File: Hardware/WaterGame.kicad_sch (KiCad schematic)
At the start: 15 parts, among them J1C1 Conn_01x07, J2 Conn_02x04_Counter_Clockwise, J4 Conn_01x02, U1 LM7805_TO220, U3 Teensy2.0_(Arduino), U4 ESP-01v090

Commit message: Hardware: Final PCB
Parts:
- removed J2: Conn_02x04_Counter_Clockwise, symbol Connector_Generic:Conn_02x04_Counter_Clockwise
- added J2: (no value), symbol Connector_Generic:Conn_02x04_Odd_Even
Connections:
- net at U6.11 (3Y): now also J2.3 (Pin_3)
- net at J1C1.1 (Pin_1), J1C1.2 (Pin_2), J1C1.3 (Pin_3)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: now also U2.1 (VI); no longer U2.2 (GND)
- net at U6.14 (4Y): now also J2.4 (Pin_4)
- net at U6.3 (1Y): now also J2.1 (Pin_1)
- net at U6.6 (2Y): now also J2.2 (Pin_2)
- net at J3.1 (Pin_1), U1.1 (VI), U5.8 (VCC2)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: now also U2.3 (VO); no longer U2.1 (VI)
- net at U5.3 (1Y): now also J2.5 (Pin_5)
- net at U5.11 (3Y): now also J2.7 (Pin_7)
- net at U5.14 (4Y): now also J2.8 (Pin_8)
- net at U5.6 (2Y): now also J2.6 (Pin_6)
- net at J5A2.4 (Pin_4), R1.2, U4.3 (CH_PD)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: now also U2.2 (GND); no longer U2.3 (VO)
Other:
- moved on the sheet: U2
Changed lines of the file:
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@@
   (junction (at 134.62 49.53) (diameter 0) (color 0 0 0 0)
   )
+  (junction (at 63.5 81.28) (diameter 0) (color 0 0 0 0)
+  )
   (junction (at 86.36 95.25) (diameter 0) (color 0 0 0 0)
   )
@@
   (junction (at 72.39 104.14) (diameter 0) (color 0 0 0 0)
   )
-  (junction (at 48.26 81.28) (diameter 0) (color 0 0 0 0)
-  )
   (junction (at 67.31 106.68) (diameter 0) (color 0 0 0 0)
   )
@@
   (junction (at 71.12 81.28) (diameter 0) (color 0 0 0 0)
   )
+  (junction (at 55.88 78.74) (diameter 0) (color 0 0 0 0)
+  )
   (junction (at 137.16 54.61) (diameter 0) (color 0 0 0 0)
   )
@@
   (junction (at 137.16 49.53) (diameter 0) (color 0 0 0 0)
   )
-  (junction (at 55.88 78.74) (diameter 0) (color 0 0 0 0)
-  )
   (junction (at 115.57 153.67) (diameter 0) (color 0 0 0 0)
   )
@@
     (stroke (width 0) (type default) (color 0 0 0 0))
   )
-  (wire (pts (xy 48.26 81.28) (xy 71.12 81.28))
+  (wire (pts (xy 48.26 81.28) (xy 63.5 81.28))
     (stroke (width 0) (type default) (color 0 0 0 0))
   )
@@
     (stroke (width 0) (type default) (color 0 0 0 0))
   )
+  (wire (pts (xy 55.88 83.82) (xy 72.39 83.82))
+    (stroke (width 0) (type default) (color 0 0 0 0))
+  )
   (wire (pts (xy 111.76 95.25) (xy 111.76 109.22))
     (stroke (width 0) (type default) (color 0 0 0 0))
@@
     (stroke (width 0) (type default) (color 0 0 0 0))
   )
-  (wire (pts (xy 55.88 78.74) (xy 55.88 81.28))
-    (stroke (width 0) (type default) (color 0 0 0 0))
-  )
   (wire (pts (xy 182.88 102.87) (xy 190.5 102.87))
     (stroke (width 0) (type default) (color 0 0 0 0))
@@
     (stroke (width 0) (type default) (color 0 0 0 0))
   )
+  (wire (pts (xy 63.5 81.28) (xy 63.5 91.44))
+    (stroke (width 0) (type default) (color 0 0 0 0))
+  )
   (wire (pts (xy 241.3 59.69) (xy 241.3 81.28))
     (stroke (width 0) (type default) (color 0 0 0 0))
@@
     (stroke (width 0) (type default) (color 0 0 0 0))
   )
-  (wire (pts (xy 63.5 88.9) (xy 72.39 88.9))
-    (stroke (width 0) (type default) (color 0 0 0 0))
-  )
   (wire (pts (xy 190.5 76.2) (xy 190.5 78.74))
     (stroke (width 0) (type default) (color 0 0 0 0))
@@
     (stroke (width 0) (type default) (color 0 0 0 0))
   )
-  (wire (pts (xy 72.39 88.9) (xy 72.39 102.87))
+  (wire (pts (xy 72.39 83.82) (xy 72.39 102.87))
     (stroke (width 0) (type default) (color 0 0 0 0))
   )
@@
     (stroke (width 0) (type default) (color 0 0 0 0))
   )
+  (wire (pts (xy 45.72 91.44) (xy 48.26 91.44))
+    (stroke (width 0) (type default) (color 0 0 0 0))
+  )
   (wire (pts (xy 175.26 73.66) (xy 182.88 73.66))
     (stroke (width 0) (type default) (color 0 0 0 0))
@@
     (stroke (width 0) (type default) (color 0 0 0 0))
   )
+  (wire (pts (xy 45.72 78.74) (xy 45.72 91.44))
+    (stroke (width 0) (type default) (color 0 0 0 0))
+  )
   (wire (pts (xy 175.26 71.12) (xy 190.5 71.12))
     (stroke (width 0) (type default) (color 0 0 0 0))
@@
     (stroke (width 0) (type default) (color 0 0 0 0))
   )
+  (wire (pts (xy 55.88 78.74) (xy 45.72 78.74))
+    (stroke (width 0) (type default) (color 0 0 0 0))
+  )
   (wire (pts (xy 102.87 138.43) (xy 107.95 138.43))
     (stroke (width 0) (type default) (color 0 0 0 0))
@@
     (stroke (width 0) (type default) (color 0 0 0 0))
   )
+  (wire (pts (xy 63.5 81.28) (xy 71.12 81.28))
+    (stroke (width 0) (type default) (color 0 0 0 0))
+  )
   (wire (pts (xy 101.6 101.6) (xy 50.8 101.6))
     (stroke (width 0) (type default) (color 0 0 0 0))
@@
   )
   (wire (pts (xy 146.05 115.57) (xy 146.05 118.11))
-    (stroke (width 0) (type default) (color 0 0 0 0))
-  )
-  (wire (pts (xy 48.26 81.28) (xy 48.26 88.9))
     (stroke (width 0) (type default) (color 0 0 0 0))
   )
@@
     (pin "8")
     (pin "9")
-  )
-  (symbol (lib_id "Connector_Generic:Conn_02x04_Counter_Clockwise") (at 100.33 161.29 270) (unit 1)
-    (in_bom yes) (on_board yes) (fields_autoplaced)
-    (property "Reference" "J2" (id 0) (at 105.41 161.2899 90)
-      (effects (font (size 1.27 1.27)) (justify left))
-    )
-    (property "Value" "Conn_02x04_Counter_Clockwise" (id 1) (at 105.41 163.8299 90)
-      (effects (font (size 1.27 1.27)) (justify left))
-    )
-    (property "Footprint" "" (id 2) (at 100.33 161.29 0)
-      (effects (font (size 1.27 1.27)) hide)
-    )
-    (property "Datasheet" "~" (id 3) (at 100.33 161.29 0)
-      (effects (font (size 1.27 1.27)) hide)
-    )
-    (pin "1")
-    (pin "2")
-    (pin "3")
-    (pin "4")
-    (pin "5")
-    (pin "6")
-    (pin "7")
-    (pin "8")
   )
   (symbol (lib_id "Connector_Generic:Conn_01x06") (at 147.32 78.74 0) (mirror x) (unit 1)
@@
     (pin "9")
   )
+  (symbol (lib_id "Connector_Generic:Conn_02x04_Odd_Even") (at 100.33 161.29 270) (unit 1)
+    (in_bom yes) (on_board yes) (fields_autoplaced)
+    (property "Reference" "J2" (id 0) (at 105.41 161.2899 90)
+      (effects (font (size 1.27 1.27)) (justify left))
+    )
+    (property "Value" "" (id 1) (at 105.41 163.8299 90)
+      (effects (font (size 1.27 1.27)) (justify left))
+    )
+    (property "Footprint" "" (id 2) (at 100.33 161.29 0)
+      (effects (font (size 1.27 1.27)) hide)
+    )
+    (property "Datasheet" "~" (id 3) (at 100.33 161.29 0)
+      (effects (font (size 1.27 1.27)) hide)
+    )
+    (pin "1")
+    (pin "2")
+    (pin "3")
+    (pin "4")
+    (pin "5")
+    (pin "6")
+    (pin "7")
+    (pin "8")
+  )
   (symbol (lib_id "Connector_Generic:Conn_01x06") (at 170.18 78.74 180) (unit 1)
     (in_bom yes) (on_board yes) (fields_autoplaced)
@@
     (pin "6")
   )
-  (symbol (lib_id "Regulator_Linear:LM7805_TO220") (at 55.88 88.9 0) (mirror x) (unit 1)
-    (in_bom yes) (on_board yes) (fields_autoplaced)
-    (property "Reference" "U2" (id 0) (at 55.88 93.98 0))
-    (property "Value" "" (id 1) (at 55.88 96.52 0))
-    (property "Footprint" "Package_TO_SOT_THT:TO-220-3_Horizontal_TabDown" (id 2) (at 55.88 94.615 0)
+  (symbol (lib_id "Regulator_Linear:LM7805_TO220") (at 55.88 91.44 0) (mirror x) (unit 1)
+    (in_bom yes) (on_board yes) (fields_autoplaced)
+    (property "Reference" "U2" (id 0) (at 55.88 96.52 0))
+    (property "Value" "" (id 1) (at 55.88 99.06 0))
+    (property "Footprint" "Package_TO_SOT_THT:TO-220-3_Horizontal_TabDown" (id 2) (at 55.88 97.155 0)
       (effects (font (size 1.27 1.27) italic) hide)
     )
-    (property "Datasheet" "https://www.onsemi.cn/PowerSolutions/document/MC7800-D.PDF" (id 3) (at 55.88 87.63 0)
+    (property "Datasheet" "https://www.onsemi.cn/PowerSolutions/document/MC7800-D.PDF" (id 3) (at 55.88 90.17 0)
       (effects (font (size 1.27 1.27)) hide)
     )
@@
       (reference "J1C1") (unit 1) (value "Conn_01x07") (footprint "Connector_PinSocket_2.54mm:PinSocket_1x07_P2.54mm_Vertical")
     )
-    (path "/40309f66-c2f3-446b-981b-5932e83e788e"
-      (reference "J2") (unit 1) (value "Conn_02x04_Counter_Clockwise") (footprint "Connector_PinSocket_2.54mm:PinSocket_2x04_P2.54mm_Vertical")
+    (path "/c8b11952-d8c2-43b2-ac25-5ad0a72cb411"
+      (reference "J2") (unit 1) (value "Conn_02x04_Odd_Even") (footprint "Connector_PinSocket_2.54mm:PinSocket_2x04_P2.54mm_Vertical")
     )
     (path "/56c30b3e-168a-4fb4-99b5-8aaef84c24d8"
@@
     )
     (path "/83b13801-99f0-4778-a16b-8dba668da6a2"
-      (reference "U4") (unit 1) (value "ESP-01v090") (footprint "Connector_PinSocket_2.54mm:PinSocket_2x04_P2.54mm_Vertical")
+      (reference "U4") (unit 1) (value "ESP-01v090") (footprint "ESP8266:ESP-01")
     )
     (path "/c81d1951-14d5-4bd3-b828-9e36a9da27e9"

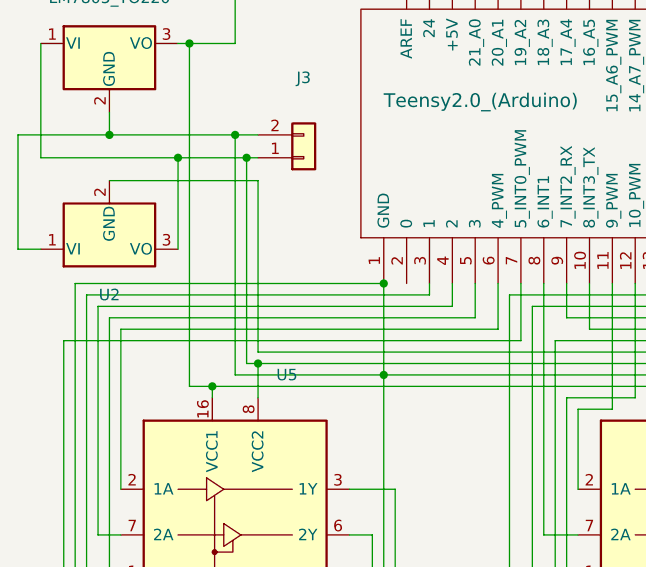
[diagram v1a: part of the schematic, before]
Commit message: Hardware: Widened high-current traces
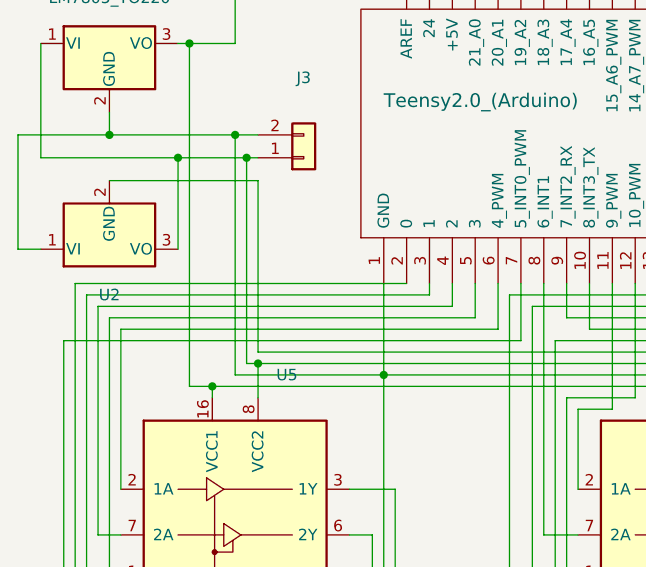
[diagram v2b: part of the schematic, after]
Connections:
- net at J1C1.1 (Pin_1), J1C1.2 (Pin_2), J1C1.3 (Pin_3)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: no longer U5.1 (EN1,2)
- net at U3.2 (0): now also U5.1 (EN1,2)
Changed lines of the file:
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@@
   (junction (at 63.5 81.28) (diameter 0) (color 0 0 0 0)
   )
-  (junction (at 86.36 95.25) (diameter 0) (color 0 0 0 0)
-  )
   (junction (at 86.36 105.41) (diameter 0) (color 0 0 0 0)
   )
@@
     (stroke (width 0) (type default) (color 0 0 0 0))
   )
+  (wire (pts (xy 52.07 95.25) (xy 88.9 95.25))
+    (stroke (width 0) (type default) (color 0 0 0 0))
+  )
   (wire (pts (xy 146.05 110.49) (xy 146.05 113.03))
     (stroke (width 0) (type default) (color 0 0 0 0))
   )
-  (wire (pts (xy 52.07 95.25) (xy 86.36 95.25))
-    (stroke (width 0) (type default) (color 0 0 0 0))
-  )

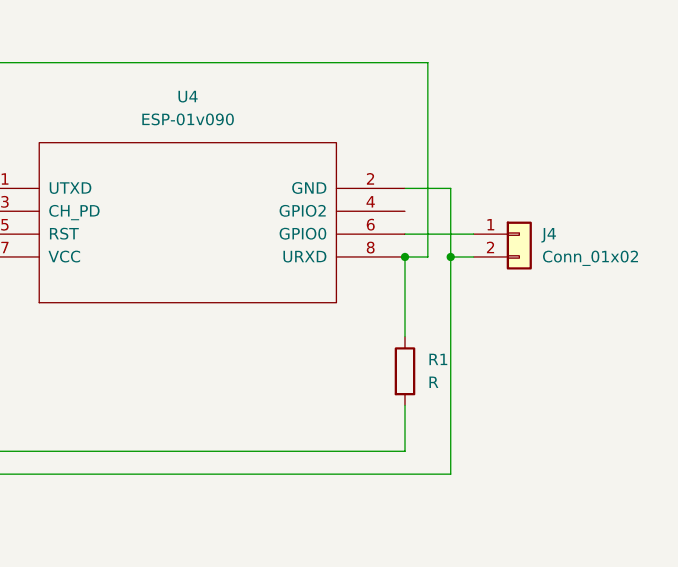
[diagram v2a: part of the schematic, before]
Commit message: Hardware: Fix ESP8266 program resistor pullup
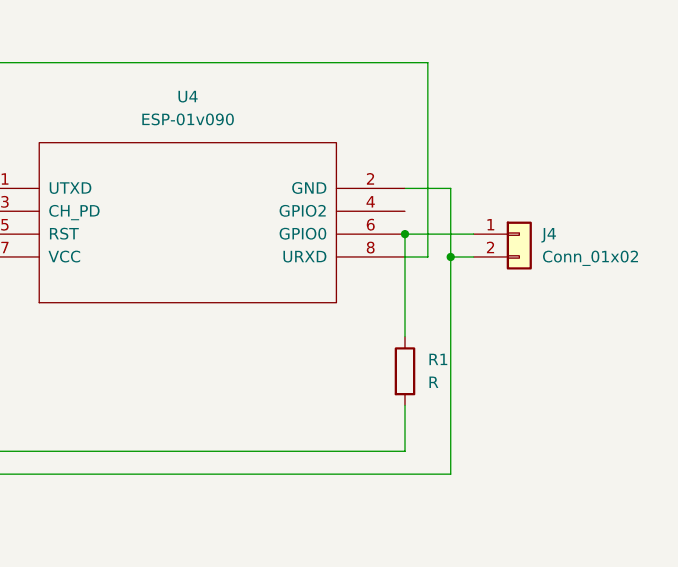
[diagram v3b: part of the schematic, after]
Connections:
- net at J4.1 (Pin_1), U4.6 (GPIO0): now also R1.1
- net at J5A2.5 (Pin_5), U4.8 (URXD): no longer R1.1
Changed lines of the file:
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@@
   (junction (at 118.11 153.67) (diameter 0) (color 0 0 0 0)
   )
-  (junction (at 238.76 81.28) (diameter 0) (color 0 0 0 0)
-  )
   (junction (at 180.34 105.41) (diameter 0) (color 0 0 0 0)
   )
@@
   (junction (at 86.36 105.41) (diameter 0) (color 0 0 0 0)
   )
+  (junction (at 238.76 78.74) (diameter 0) (color 0 0 0 0)
+  )
   (junction (at 182.88 102.87) (diameter 0) (color 0 0 0 0)
   )
@@
     (stroke (width 0) (type default) (color 0 0 0 0))
   )
+  (wire (pts (xy 238.76 78.74) (xy 238.76 90.17))
+    (stroke (width 0) (type default) (color 0 0 0 0))
+  )
   (wire (pts (xy 63.5 81.28) (xy 63.5 91.44))
     (stroke (width 0) (type default) (color 0 0 0 0))
@@
     (stroke (width 0) (type default) (color 0 0 0 0))
   )
-  (wire (pts (xy 238.76 81.28) (xy 238.76 90.17))
-    (stroke (width 0) (type default) (color 0 0 0 0))
-  )

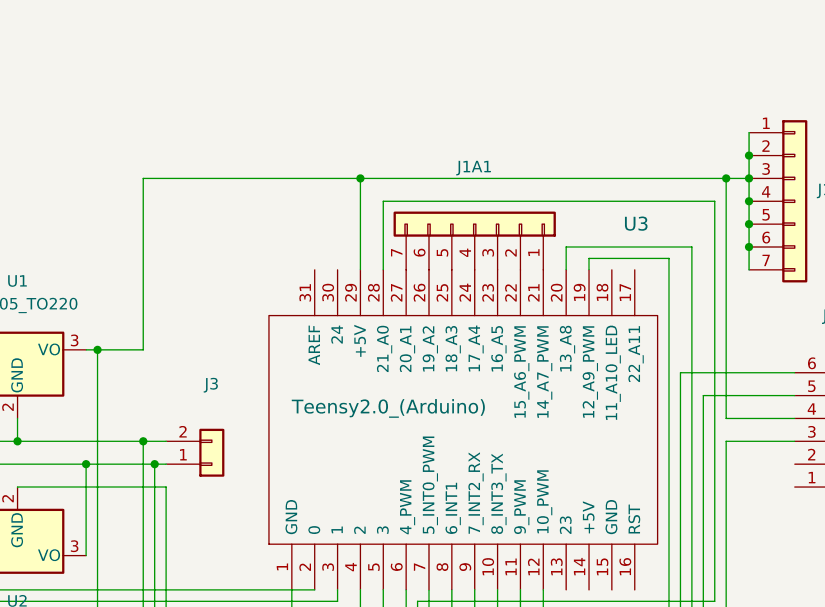
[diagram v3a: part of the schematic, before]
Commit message: Hardware: Add dedicated status LED
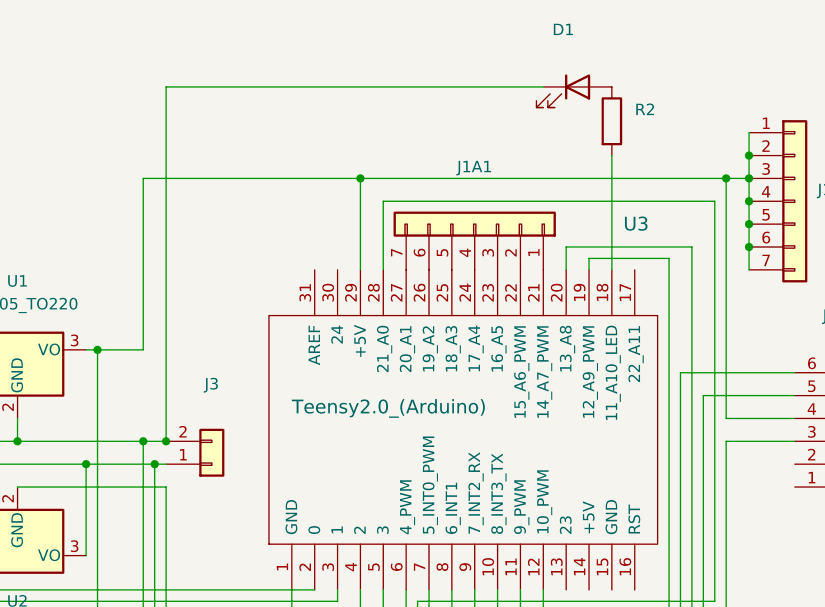
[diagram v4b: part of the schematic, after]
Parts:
- added D1: (no value), symbol Device:LED
- added R2: (no value), symbol Device:R
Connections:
- net at J1C1.1 (Pin_1), J1C1.2 (Pin_2), J1C1.3 (Pin_3)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: now also D1.1 (K)
- net at U3.18 (11_A10_LED): now also R2.2
- new net: D1.2 (A), R2.1
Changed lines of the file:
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@@
   (junction (at 137.16 57.15) (diameter 0) (color 0 0 0 0)
   )
+  (junction (at 72.39 78.74) (diameter 0) (color 0 0 0 0)
+  )
   (junction (at 118.11 153.67) (diameter 0) (color 0 0 0 0)
   )
@@
     (stroke (width 0) (type default) (color 0 0 0 0))
   )
+  (wire (pts (xy 72.39 78.74) (xy 72.39 39.37))
+    (stroke (width 0) (type default) (color 0 0 0 0))
+  )
   (wire (pts (xy 190.5 76.2) (xy 190.5 78.74))
     (stroke (width 0) (type default) (color 0 0 0 0))
@@
     (stroke (width 0) (type default) (color 0 0 0 0))
   )
+  (wire (pts (xy 72.39 39.37) (xy 114.3 39.37))
+    (stroke (width 0) (type default) (color 0 0 0 0))
+  )
   (wire (pts (xy 243.84 105.41) (xy 243.84 81.28))
     (stroke (width 0) (type default) (color 0 0 0 0))
@@
   )
   (wire (pts (xy 146.05 110.49) (xy 146.05 113.03))
+    (stroke (width 0) (type default) (color 0 0 0 0))
+  )
+  (wire (pts (xy 121.92 46.99) (xy 121.92 59.69))
     (stroke (width 0) (type default) (color 0 0 0 0))
   )
@@
     (pin "6")
     (pin "7")
+  )
+  (symbol (lib_id "Device:R") (at 121.92 43.18 0) (unit 1)
+    (in_bom yes) (on_board yes) (fields_autoplaced)
+    (property "Reference" "R2" (id 0) (at 124.46 41.9099 0)
+      (effects (font (size 1.27 1.27)) (justify left))
+    )
+    (property "Value" "" (id 1) (at 124.46 44.4499 0)
+      (effects (font (size 1.27 1.27)) (justify left))
+    )
+    (property "Footprint" "" (id 2) (at 120.142 43.18 90)
+      (effects (font (size 1.27 1.27)) hide)
+    )
+    (property "Datasheet" "~" (id 3) (at 121.92 43.18 0)
+      (effects (font (size 1.27 1.27)) hide)
+    )
+    (pin "1")
+    (pin "2")
   )
   (symbol (lib_id "teensy:Teensy2.0_(Arduino)") (at 105.41 77.47 90) (unit 1)
@@
     (pin "8")
   )
+  (symbol (lib_id "Device:LED") (at 118.11 39.37 0) (unit 1)
+    (in_bom yes) (on_board yes) (fields_autoplaced)
+    (property "Reference" "D1" (id 0) (at 116.5225 33.02 0))
+    (property "Value" "" (id 1) (at 116.5225 35.56 0))
+    (property "Footprint" "" (id 2) (at 118.11 39.37 0)
+      (effects (font (size 1.27 1.27)) hide)
+    )
+    (property "Datasheet" "~" (id 3) (at 118.11 39.37 0)
+      (effects (font (size 1.27 1.27)) hide)
+    )
+    (pin "1")
+    (pin "2")
+  )
   (symbol (lib_id "Connector_Generic:Conn_01x06") (at 170.18 78.74 180) (unit 1)
     (in_bom yes) (on_board yes) (fields_autoplaced)
@@
   )
   (symbol_instances
+    (path "/d0aa7f92-a576-4787-bc24-eb0010d6ee3c"
+      (reference "D1") (unit 1) (value "LED") (footprint "LED_THT:LED_D5.0mm")
+    )
     (path "/c6fdc430-486c-47b4-8431-6aa30e8f73f5"
       (reference "J1A1") (unit 1) (value "Conn_01x07") (footprint "Connector_PinSocket_2.54mm:PinSocket_1x07_P2.54mm_Vertical")
@@
       (reference "R1") (unit 1) (value "R") (footprint "Resistor_THT:R_Axial_DIN0204_L3.6mm_D1.6mm_P7.62mm_Horizontal")
     )
+    (path "/b677ba33-ca11-4deb-8646-6143211c20c4"
+      (reference "R2") (unit 1) (value "R") (footprint "Resistor_THT:R_Axial_DIN0204_L3.6mm_D1.6mm_P7.62mm_Horizontal")
+    )
     (path "/79c7287d-4b2c-40be-9c6d-d6fb14577bc7"
